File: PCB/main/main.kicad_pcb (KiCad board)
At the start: 2 copper layers, 96 x 70 mm, 83 parts, among them IC1 TP4056-42-ESOP8, IC2 LM393DR2G, IC3 AT24C256C-SSHL-T, IC4 TXS0108EPWR, J10 Conn_01x02_Male, J11 Conn_01x02_Male, J12 Conn_01x02_Male, J13 Conn_01x02_Male, J2 Conn_01x33_Female, J3 Conn_01x33_Female, J5 MICROXNJ, J6 Conn_01x02_Male, J7 Conn_01x02_Male, J8 Conn_01x02_Male, J9 Conn_01x02_Male, Q1 MMBT3904, Q2 AO3401A, U1 HT75xx-1-SOT89, U2 DS18B20Z, U3 ALS-PDIC15-21B/TR8, U4 CH340G, Y1 YSX321SL

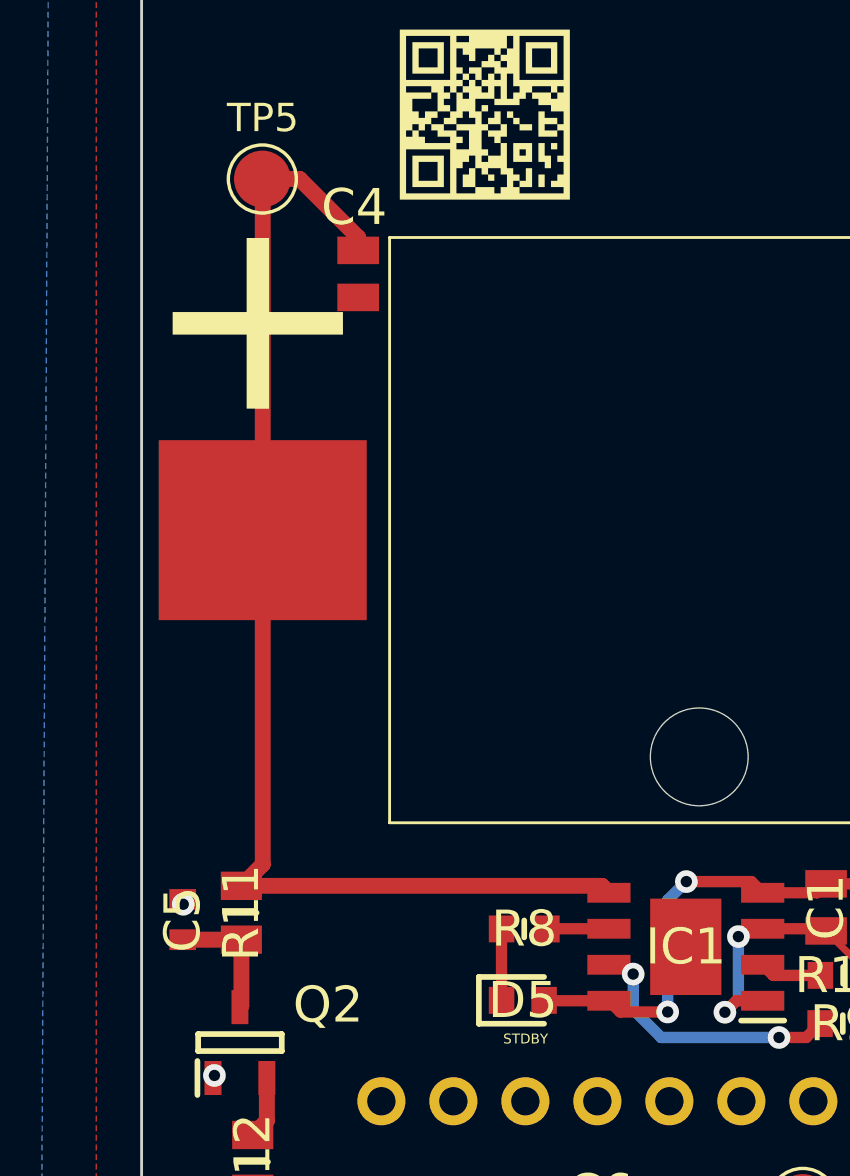
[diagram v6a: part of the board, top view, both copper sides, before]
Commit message: Updated v1.0 - moved a decouplicng capacitor closer to pin
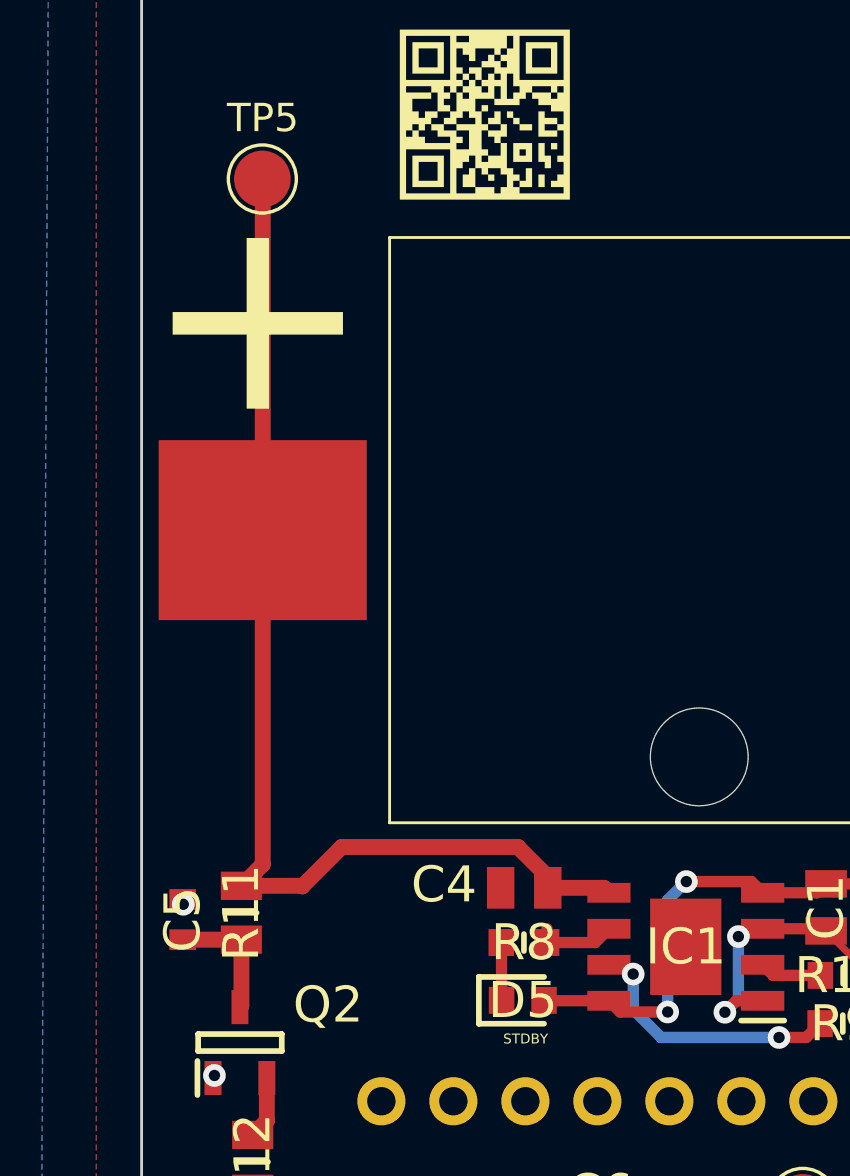
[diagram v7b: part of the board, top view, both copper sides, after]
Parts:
- moved C4 22.4 mm to (103.2, 117.2), turned to 180 degrees
- moved R8 0.48 mm to (103.2, 119.1)
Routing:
- net /Power/BAT +: track 43.1 -> 39.8 mm
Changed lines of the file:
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@@
   )
   (footprint "10uF_0804:CAPC2012X145N" (layer "F.Cu")
-    (at 97.34 95.51 -90)
+    (at 103.2 117.17 180)
     (descr "CL21A106KAYNNNE")
     (tags "Capacitor")
@@
     (property "Sheetname" "Power")
     (attr smd)
-    (fp_text reference "C4" (at -2.35 0.14 180) (layer "F.SilkS")
-      (effects (font (size 1.27 1.27) (thickness 0.254)))
-    )
-    (fp_text value "10uF" (at 0 0 90) (layer "F.SilkS") hide
-      (effects (font (size 1.27 1.27) (thickness 0.254)))
-    )
-    (fp_text user "${REFERENCE}" (at 0 0 90) (layer "F.Fab")
+    (fp_text reference "C4" (at 2.83 0.11 180) (layer "F.SilkS")
+      (effects (font (size 1.27 1.27) (thickness 0.254)))
+    )
+    (fp_text value "10uF" (at 0 0) (layer "F.SilkS") hide
+      (effects (font (size 1.27 1.27) (thickness 0.254)))
+    )
+    (fp_text user "${REFERENCE}" (at 0 0) (layer "F.Fab")
       (effects (font (size 1.27 1.27) (thickness 0.254)))
     )
@@
     (fp_line (start -1 -0.625) (end 1 -0.625) (layer "F.Fab") (width 0.1))
     (fp_line (start 1 0.625) (end -1 0.625) (layer "F.Fab") (width 0.1))
-    (pad "1" smd rect locked (at -0.83 0 270) (size 0.97 1.47) (layers "F.Cu" "F.Paste" "F.Mask")
+    (pad "1" smd rect locked (at -0.83 0 180) (size 0.97 1.47) (layers "F.Cu" "F.Paste" "F.Mask")
       (net 71 "/Power/BAT +") (pintype "passive"))
-    (pad "2" smd rect locked (at 0.83 0 270) (size 0.97 1.47) (layers "F.Cu" "F.Paste" "F.Mask")
+    (pad "2" smd rect locked (at 0.83 0 180) (size 0.97 1.47) (layers "F.Cu" "F.Paste" "F.Mask")
       (net 2 "GND") (pintype "passive"))
     (model "CL21A106KAYNNNE.stp"
@@
   )
   (footprint "1k:RESC1608X55N" (layer "F.Cu")
-    (at 103.2 118.62)
+    (at 103.19 119.1)
     (descr "1.6mmx0.8mm")
     (tags "Resistor")
@@
   (segment (start 105.29 138.14) (end 105.3 138.14) (width 0.4) (layer "B.Cu") (net 70))
   (segment (start 105.3 138.14) (end 105.91 138.14) (width 0.4) (layer "B.Cu") (net 70))
-  (segment (start 97.34 94.68) (end 97.34 94.22) (width 0.56) (layer "F.Cu") (net 71))
   (segment (start 93.975 116.345) (end 93.22 117.1) (width 0.56) (layer "F.Cu") (net 71))
   (segment (start 93.975 92.225) (end 93.975 104.55) (width 0.56) (layer "F.Cu") (net 71))
-  (segment (start 93.22 117.1) (end 105.943 117.1) (width 0.56) (layer "F.Cu") (net 71))
-  (segment (start 97.34 94.22) (end 95.28 92.16) (width 0.56) (layer "F.Cu") (net 71))
+  (segment (start 96.76 115.73) (end 95.37 117.12) (width 0.56) (layer "F.Cu") (net 71))
+  (segment (start 104.03 116.78) (end 102.98 115.73) (width 0.56) (layer "F.Cu") (net 71))
+  (segment (start 104.03 117.17) (end 104.03 116.78) (width 0.56) (layer "F.Cu") (net 71))
   (segment (start 93.96 92.16) (end 93.91 92.16) (width 0.56) (layer "F.Cu") (net 71))
-  (segment (start 105.943 117.1) (end 106.188 117.345) (width 0.56) (layer "F.Cu") (net 71))
-  (segment (start 93.96 92.16) (end 95.28 92.16) (width 0.56) (layer "F.Cu") (net 71))
+  (segment (start 95.37 117.12) (end 95.35 117.1) (width 0.56) (layer "F.Cu") (net 71))
+  (segment (start 102.98 115.73) (end 96.76 115.73) (width 0.56) (layer "F.Cu") (net 71))
+  (segment (start 95.35 117.1) (end 93.22 117.1) (width 0.56) (layer "F.Cu") (net 71))
+  (segment (start 106.013 117.17) (end 106.188 117.345) (width 0.56) (layer "F.Cu") (net 71))
+  (segment (start 104.03 117.17) (end 106.013 117.17) (width 0.56) (layer "F.Cu") (net 71))
   (segment (start 93.975 104.55) (end 93.975 116.345) (width 0.56) (layer "F.Cu") (net 71))
   (segment (start 93.91 92.16) (end 93.975 92.225) (width 0.56) (layer "F.Cu") (net 71))
-  (segment (start 106.188 118.615) (end 104.005 118.615) (width 0.4) (layer "F.Cu") (net 72))
+  (segment (start 103.99 119.1) (end 105.703 119.1) (width 0.4) (layer "F.Cu") (net 72))
+  (segment (start 105.703 119.1) (end 106.188 118.615) (width 0.4) (layer "F.Cu") (net 72))
   (segment (start 104.005 118.615) (end 104 118.62) (width 0.4) (layer "F.Cu") (net 72))
   (segment (start 113.15 122.45) (end 113.64 121.96) (width 0.4) (layer "F.Cu") (net 73))
@@
   (segment (start 143.13 119.26) (end 143.08 119.31) (width 0.4) (layer "F.Cu") (net 115))
   (segment (start 128.0945 121.666) (end 125.41 121.666) (width 0.4) (layer "F.Cu") (net 116))
-  (segment (start 102.4 121.14) (end 102.4 118.62) (width 0.4) (layer "F.Cu") (net 117))
+  (segment (start 102.4 119.11) (end 102.39 119.1) (width 0.4) (layer "F.Cu") (net 117))
+  (segment (start 102.4 121.14) (end 102.4 119.11) (width 0.4) (layer "F.Cu") (net 117))
   (segment (start 112.97 134) (end 112.97 134.425) (width 0.4) (layer "F.Cu") (net 118))
   (segment (start 111.410766 133.35) (end 112.32 133.35) (width 0.4) (layer "F.Cu") (net 118))

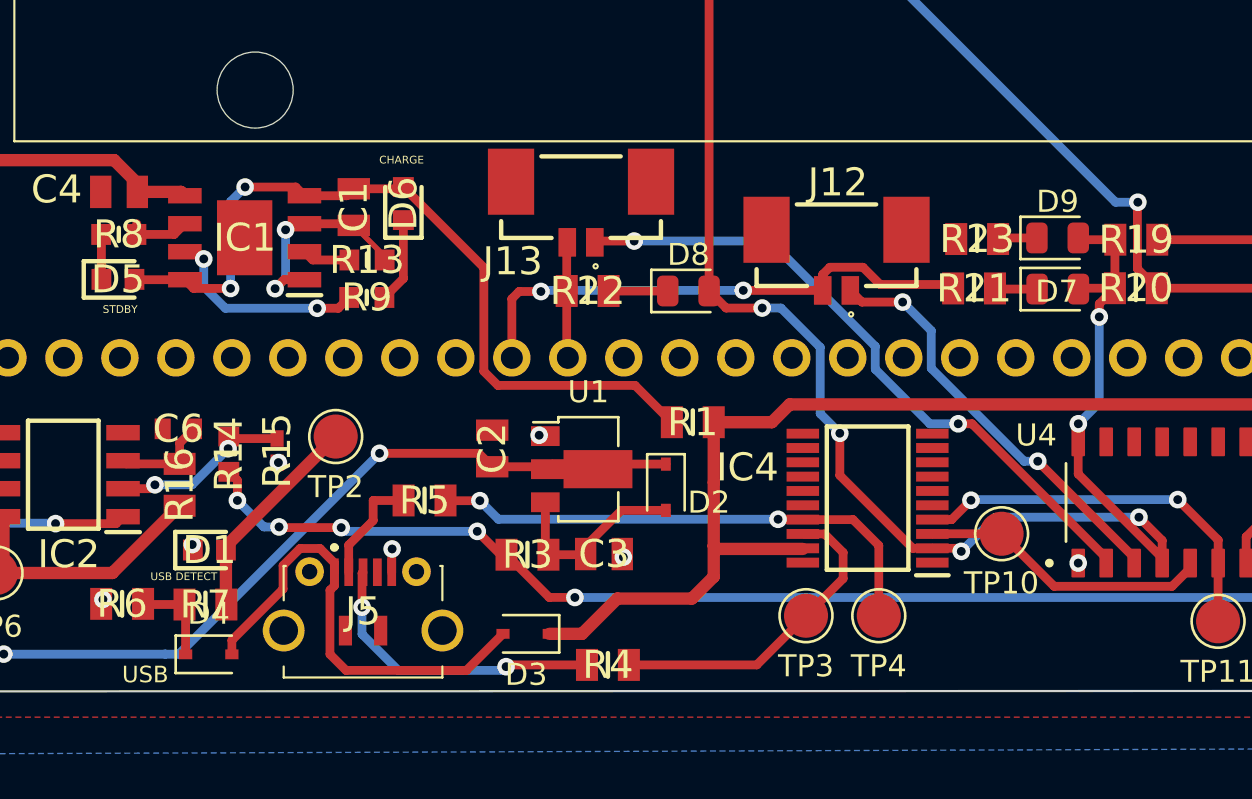
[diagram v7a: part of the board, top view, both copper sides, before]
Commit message: Updates to Microcontroller Circuit
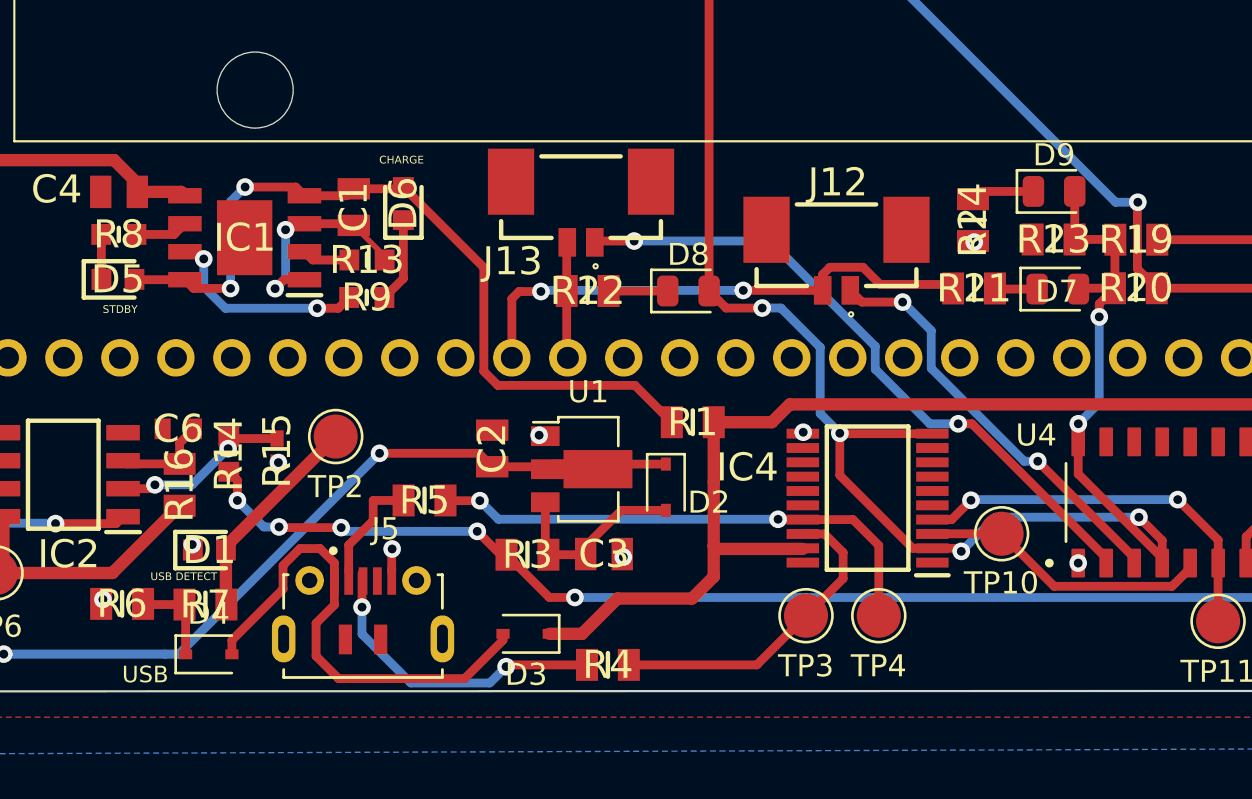
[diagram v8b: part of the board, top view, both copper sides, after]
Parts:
- added R24: 1.5k, 4k7:RESC2013X65N, F.Cu at (141.9, 118.5)
- J5: footprint 3088_power:MICROXNJ -> 3088_power:SHOUHAN_MICROXNJ
- moved R23 3.47 mm to (145.6, 119.3)
- moved D9 2.12 mm to (145.6, 117.2)
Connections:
- IC4 pad 10: unconnected-(IC4-Pad10) -> +3V3
- IC4 pad 11: unconnected-(IC4-Pad11) -> GND
- R23 pad 2: Net-(D9-Pad1) -> +3V3
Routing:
- net +3V3: track 128.6 -> 135.1 mm
- net Net-(D3-Pad2): track 21.0 -> 22.6 mm
- net Net-(D9-Pad1): track 1.78 -> 2.89 mm
- net GND: track 14.7 -> 14.8 mm, vias 17 -> 19
